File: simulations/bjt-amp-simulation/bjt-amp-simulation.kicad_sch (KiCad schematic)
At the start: 11 parts, among them Q1 BJT

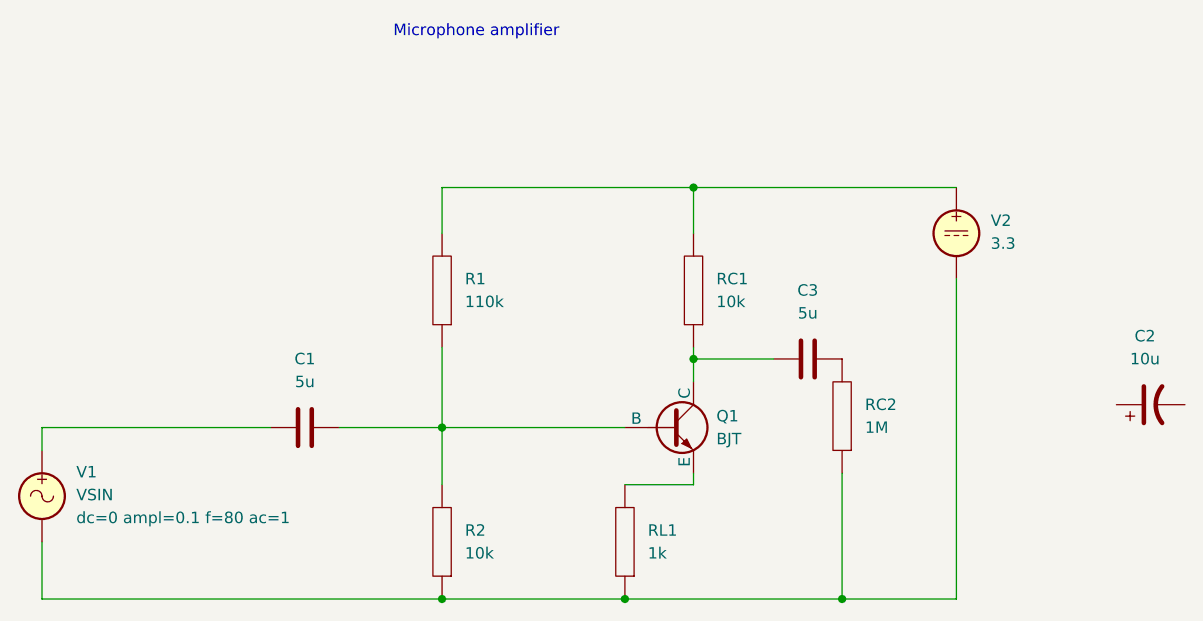
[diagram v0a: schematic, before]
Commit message: [bjt-amp-calc bjt-amp-simulation schematics] Impl | Validated amplifier design
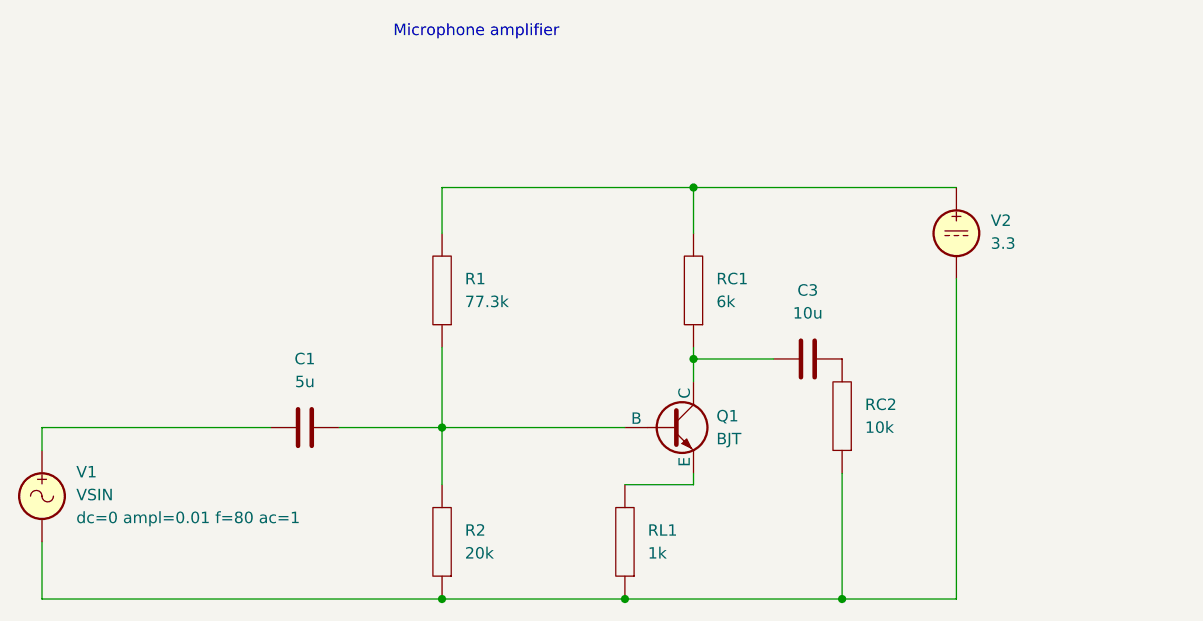
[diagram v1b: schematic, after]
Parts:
- removed C2: 10u, symbol Device:C_Polarized_US
- C3: value 5u -> 10u
- R1: value 110k -> 77.3k
- R2: value 10k -> 20k
- RC1: value 10k -> 6k
- RC2: value 1M -> 10k
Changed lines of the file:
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@@
 			)
 		)
-		(property "Value" "1M"
+		(property "Value" "10k"
 			(at 172.72 92.7099 0)
 			(effects
@@
 			)
 		)
-		(property "Value" "10k"
+		(property "Value" "6k"
 			(at 156.21 78.7399 0)
 			(effects
@@
 			)
 		)
-		(property "Sim.Params" "dc=0 ampl=0.1 f=80 ac=1"
+		(property "Sim.Params" "dc=0 ampl=0.01 f=80 ac=1"
 			(at 85.09 102.7402 0)
 			(effects
@@
 			)
 		)
-		(property "Value" "5u"
+		(property "Value" "10u"
 			(at 166.37 80.01 90)
 			(effects
@@
 			)
 		)
-		(property "Value" "110k"
+		(property "Value" "77.3k"
 			(at 128.27 78.7399 0)
 			(effects
@@
 			)
 		)
-		(property "Value" "10k"
+		(property "Value" "20k"
 			(at 128.27 106.6799 0)
 			(effects
@@
 					(unit 1)
 				)
-			)
-		)
-	)
-	(symbol
-		(lib_id "Device:C_Polarized_US")
-		(at 204.47 90.17 90)
-		(unit 1)
-		(exclude_from_sim no)
-		(in_bom yes)
-		(on_board yes)
-		(dnp no)
-		(fields_autoplaced yes)
-		(property "Reference" "C2"
-			(at 203.835 82.55 90)
-			(effects
-				(font
-					(size 1.27 1.27)
-				)
-			)
-		)
-		(property "Value" "10u"
-			(at 203.835 85.09 90)
-			(effects
-				(font
-					(size 1.27 1.27)
-				)
-			)
-		)
-		(property "Footprint" ""
-			(at 204.47 90.17 0)
-			(effects
-				(font
-					(size 1.27 1.27)
-				)
-				(hide yes)
-			)
-		)
-		(property "Datasheet" "~"
-			(at 204.47 90.17 0)
-			(effects
-				(font
-					(size 1.27 1.27)
-				)
-				(hide yes)
-			)
-		)
-		(property "Description" "Polarized capacitor, US symbol"
-			(at 204.47 90.17 0)
-			(effects
-				(font
-					(size 1.27 1.27)
-				)
-				(hide yes)
-			)
-		)
-		(pin "2"
-		)
-		(pin "1"
-		)
-		(instances
-			(project "bjt-amp-simulation"
-				(path "/7eb2004b-dcea-4027-b257-90c715ab0ad6"
-					(reference "C2")
-					(unit 1)
-				)
